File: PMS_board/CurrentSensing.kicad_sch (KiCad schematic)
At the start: 0 parts

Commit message: Added Current Sensing
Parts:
- added C40, C41, C42, C43, C44: 0.1uF, symbol Device:C
- added R36, R37, R38, R39, R40: 0.5m, Package_SON:WSON-8-1EP_6x5mm_P1.27mm_EP3.4x4mm, symbol Device:R_Shunt_US
- added U14, U15, U16, U17, U9: INA186A2QDCKRQ1, DCK0006A-IPC_A, symbol Symbols:INA186A2QDCKRQ1
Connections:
- new net: R36.2, U9.4 (IN+)
- new net: R36.3, U9.5 (IN-)
- new net: R37.2, U14.4 (IN+)
- new net: R37.3, U14.5 (IN-)
- new net: R38.2, U15.4 (IN+)
- new net: R38.3, U15.5 (IN-)
- new net: R40.2, U17.4 (IN+)
- new net: R40.3, U17.5 (IN-)
- new net: R39.2, U16.4 (IN+)
- new net: R39.3, U16.5 (IN-)
- new net +12V: R40.1
- new net +24V: R39.1
- new net +3.3V: C40.1, C41.1, C42.1, C43.1, C44.1, U14.3 (VS), U15.3 (VS), U16.3 (VS), U17.3 (VS), U9.3 (VS)
- new net AUX_OUT: R37.4
- new net AUX_SENSE: U14.6 (OUT)
- new net BATT_IN: R36.1
- new net BATT_OUT: R36.4
- new net BATT_SENSE: U9.6 (OUT)
- new net BOARD_OUT: R38.4
- new net BOARD_SENSE: U15.6 (OUT)
- new net GND: C40.2, C41.2, C42.2, C43.2, C44.2, U14.1 (REF), U14.2 (GND), U15.1 (REF), U15.2 (GND), U16.1 (REF), U16.2 (GND), U17.1 (REF), U17.2 (GND), U9.1 (REF), U9.2 (GND)
- new net JET_OUT: R40.4
- new net JET_SENSE: U17.6 (OUT)
- new net NET_OUT: R39.4
- new net NET_SENSE: U16.6 (OUT)
- new net PACK+: R37.1, R38.1

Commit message: Changed shunt resistor values to be more accurate
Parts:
- R36: value 0.5m -> 0.2m
- R37: value 0.5m -> 2m
- R38, R40: value 0.5m -> 10m
- R39: value 0.5m -> 50m
- U14, U15, U17: value INA186A2QDCKRQ1 -> INA186A2IDCK
- U16: value INA186A2QDCKRQ1 -> INA186A1IDCK
- U9: value INA186A2QDCKRQ1 -> INA186A3IDCK
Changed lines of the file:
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@@
 			)
 		)
-		(property "Value" "0.5m"
+		(property "Value" "0.2m"
 			(at 17.78 59.6899 0)
 			(show_name no)
@@
 			)
 		)
-		(property "Value" "0.5m"
+		(property "Value" "2m"
 			(at 101.6 60.9599 0)
 			(show_name no)
@@
 			)
 		)
-		(property "Value" "INA186A2QDCKRQ1"
+		(property "Value" "INA186A3IDCK"
 			(at 57.15 43.18 0)
 			(show_name no)
@@
 			)
 		)
-		(property "Value" "0.5m"
+		(property "Value" "10m"
 			(at 181.61 60.9599 0)
 			(show_name no)
@@
 			)
 		)
-		(property "Value" "INA186A2QDCKRQ1"
+		(property "Value" "INA186A2IDCK"
 			(at 140.97 109.22 0)
 			(show_name no)
@@
 			)
 		)
-		(property "Value" "0.5m"
+		(property "Value" "50m"
 			(at 17.78 124.4599 0)
 			(show_name no)
@@
 			)
 		)
-		(property "Value" "INA186A2QDCKRQ1"
+		(property "Value" "INA186A2IDCK"
 			(at 140.97 44.45 0)
 			(show_name no)
@@
 			)
 		)
-		(property "Value" "INA186A2QDCKRQ1"
+		(property "Value" "INA186A2IDCK"
 			(at 220.98 44.45 0)
 			(show_name no)
@@
 			)
 		)
-		(property "Value" "INA186A2QDCKRQ1"
+		(property "Value" "INA186A1IDCK"
 			(at 57.15 107.95 0)
 			(show_name no)
@@
 			)
 		)
-		(property "Value" "0.5m"
+		(property "Value" "10m"
 			(at 101.6 125.7299 0)
 			(show_name no)

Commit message: Added ADC for current sensing
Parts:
- removed C41: 0.1uF, symbol Device:C
- removed R37: 2m, Package_SON:WSON-8-1EP_6x5mm_P1.27mm_EP3.4x4mm, symbol Device:R_Shunt_US
- removed U14: INA186A2IDCK, DCK0006A-IPC_A, symbol Symbols:INA186A2QDCKRQ1
- added U18: MCP3204T-CI/ST, Package_DFN_QFN:QFN-20-1EP_5x5mm_P0.65mm_EP3.35x3.35mm, symbol Analog_ADC:MCP3204
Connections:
- net +3.3V: now also U18.13 (Vref), U18.14 (Vdd)
- net BATT_SENSE: now also U18.1 (CH0)
- net GND: now also U18.12 (AGND), U18.7 (DGND)
- net JET_SENSE: now also U18.4 (CH3)
- net NET_SENSE: now also U18.3 (CH2)
- net BOARD_SENSE renamed CORE_SENSE
- net CORE_SENSE: now also U18.2 (CH1)
- new net CLK: U18.11 (CLK)
- new net CS: U18.8 (~{CS}/SHDN)
- new net Din: U18.9 (Din)
- new net Dout: U18.10 (Dout)
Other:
- moved on the sheet: C42, R38, U15

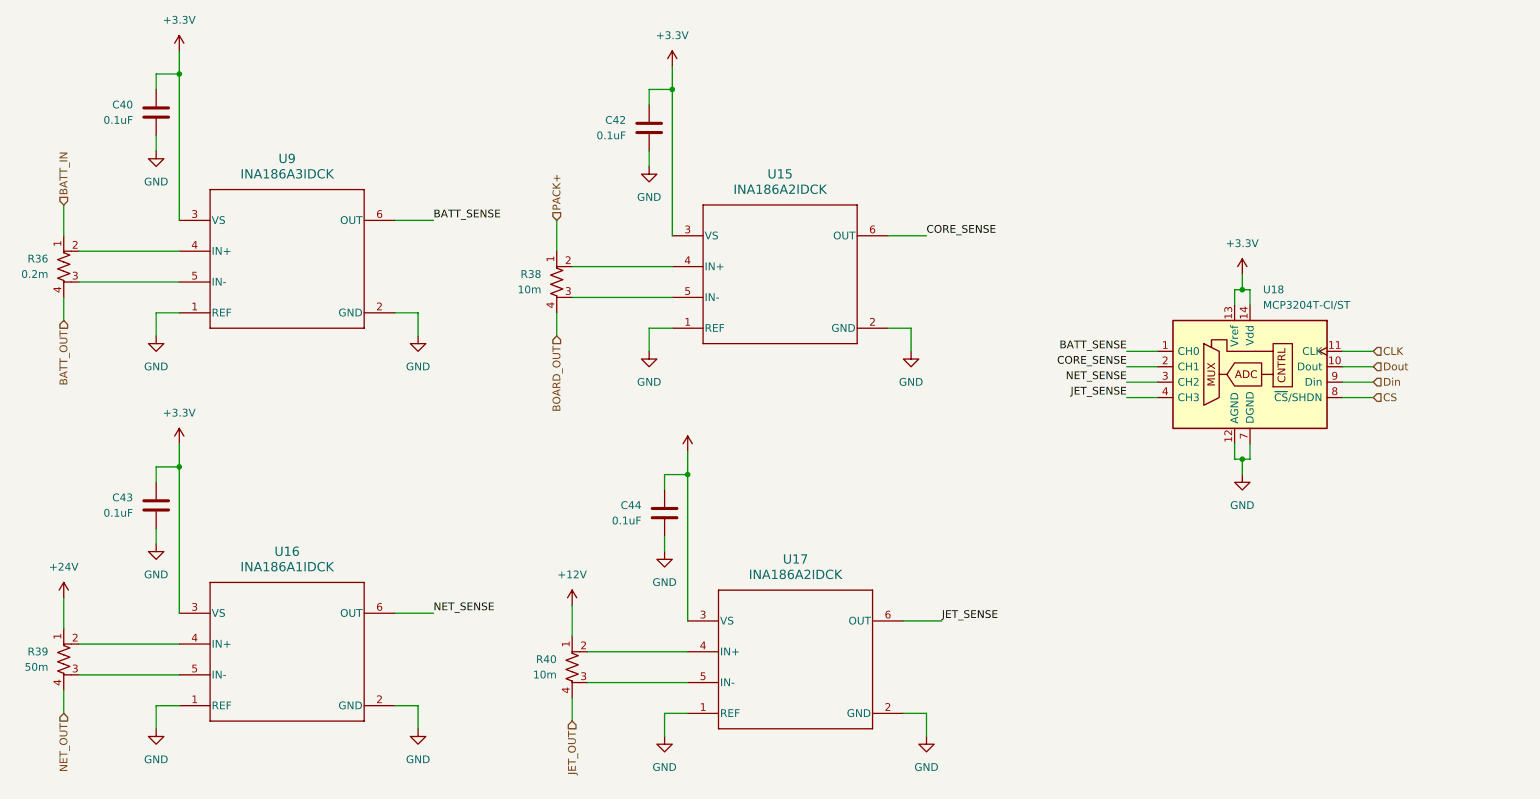
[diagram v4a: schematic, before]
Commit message: Refine Current Sensing
- Removed redundant current sensors
- Fixed hierarchical labelling for sensors
- added labeling for a few circuits
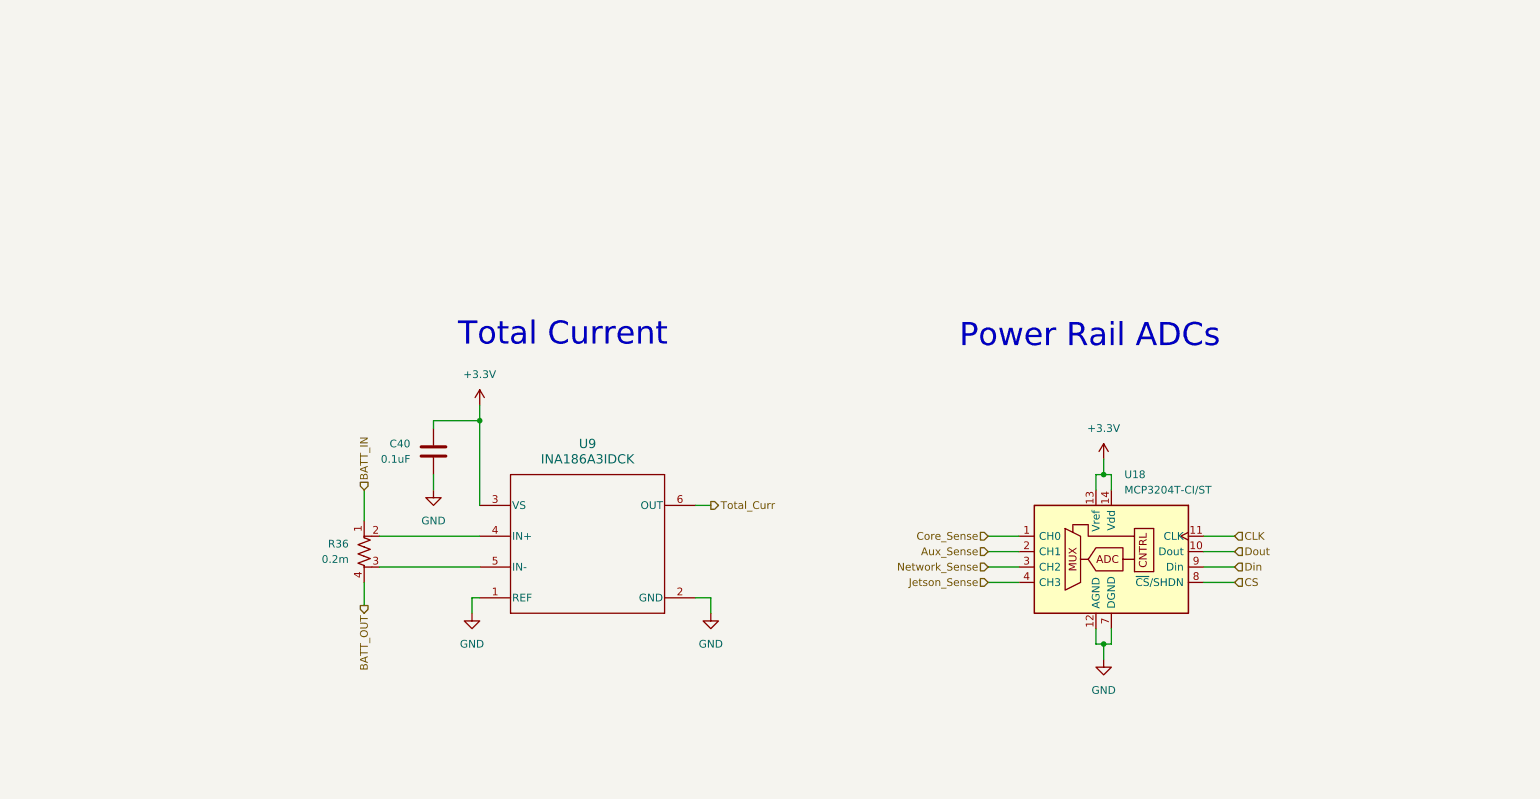
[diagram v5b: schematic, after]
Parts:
- removed C42, C43, C44: 0.1uF, symbol Device:C
- removed R38, R40: 10m, Package_SON:WSON-8-1EP_6x5mm_P1.27mm_EP3.4x4mm, symbol Device:R_Shunt_US
- removed R39: 50m, Package_SON:WSON-8-1EP_6x5mm_P1.27mm_EP3.4x4mm, symbol Device:R_Shunt_US
- removed U15, U17: INA186A2IDCK, DCK0006A-IPC_A, symbol Symbols:INA186A2QDCKRQ1
- removed U16: INA186A1IDCK, DCK0006A-IPC_A, symbol Symbols:INA186A2QDCKRQ1
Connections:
- net BATT_SENSE renamed Core_Sense
- net Core_Sense: no longer U9.6 (OUT)
- net CORE_SENSE renamed Aux_Sense
- net JET_SENSE renamed Jetson_Sense
- net NET_SENSE renamed Network_Sense
- new net Total_Curr: U9.6 (OUT)
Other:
- note added: "Power Rail ADCs"
- note added: "Total Current"
- moved on the sheet: C40, R36, U18, U9

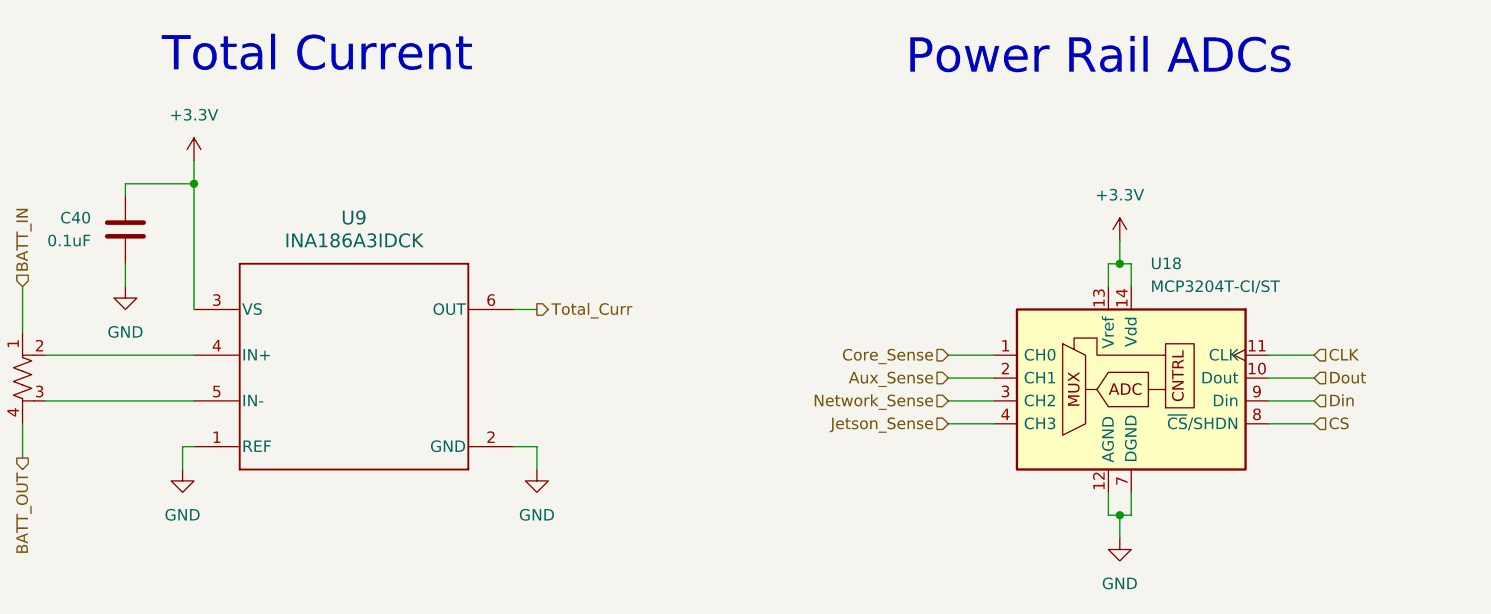
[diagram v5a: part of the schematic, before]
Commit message: Finish Schematic
There's definitely stuff I missed, but I'm tired so we can review later. For my members to keep track of things, these are the changes/last minute additions I ran out of time to teach:
- brake chopper circuitry & reverse voltage protection for aux & motor rails
- microcontroller pinnouts
- net connections between sheets
- voltage resistors & system voltage measurements
- cell sense connectors & switch
- ADC routing
Please Please PLEASE ask questions about these additions. I don't want you guys to feel like you don't own this schematic, and I'm sorry I had to take away some of these designs to finish early. I definitely left too much on your plate to get everything perfect, which is my bad. I will happily walk through each and every circuit and help explain each part so you can better know your project when we get to reviewing and debugging later down the line.
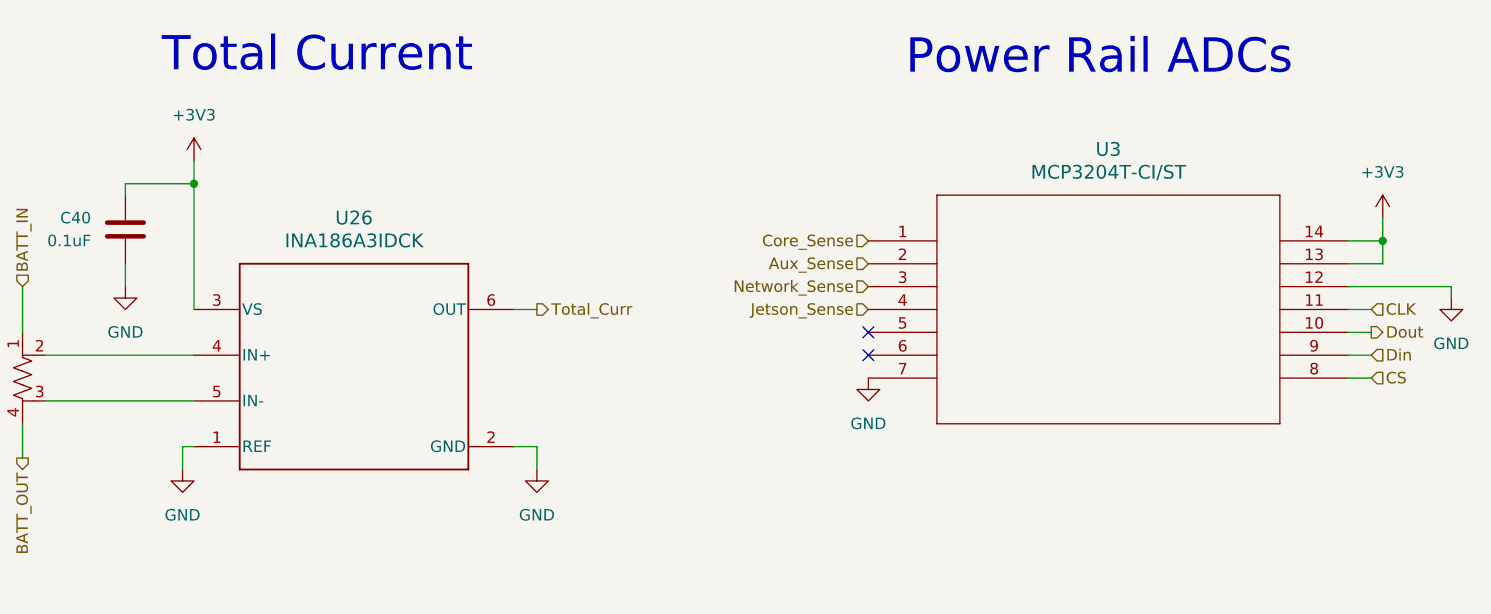
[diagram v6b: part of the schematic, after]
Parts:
- removed U18: MCP3204T-CI/ST, Package_DFN_QFN:QFN-20-1EP_5x5mm_P0.65mm_EP3.35x3.35mm, symbol Analog_ADC:MCP3204
- removed U9: INA186A3IDCK, DCK0006A-IPC_A, symbol Symbols:INA186A2QDCKRQ1
- added U26: INA186A3IDCK, DCK0006A-IPC_A, symbol Symbols:INA186A2QDCKRQ1
- added U3: MCP3204T-CI/ST, TSSOP14_MC_MCH, symbol MCP3204T-CIST:MCP3204T-CI_ST
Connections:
- net Aux_Sense: now also U3.2
- net CLK: now also U3.11
- net CS: now also U3.8
- net Core_Sense: now also U3.1
- net Din: now also U3.9
- net Dout: now also U3.10
- net GND: now also U26.1 (REF), U26.2 (GND), U3.12, U3.7
- net Jetson_Sense: now also U3.4
- net Network_Sense: now also U3.3
- net Total_Curr: now also U26.6 (OUT)
- net at R36.2: now also U26.4 (IN+)
- net at R36.3: now also U26.5 (IN-)
- net +3.3V renamed +3V3
- net +3V3: now also U26.3 (VS), U3.13, U3.14
- no-connect marks 0 -> 2

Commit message: Add Footprints & such
whoops forgot to push yesterday teehee
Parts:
- C40: footprint (none) -> Capacitor_SMD:C_0603_1608Metric
- U26: footprint DCK0006A-IPC_A -> INA186A3IDCK:SO8_DCK_TEX
- U3: footprint TSSOP14_MC_MCH -> MCP3204T-CIST:TSSOP14_MC_MCH
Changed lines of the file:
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@@
 			)
 		)
-		(property "Footprint" ""
+		(property "Footprint" "Capacitor_SMD:C_0603_1608Metric"
 			(at 80.3148 92.71 0)
 			(hide yes)
@@
 			)
 		)
-		(property "Footprint" "TSSOP14_MC_MCH"
+		(property "Footprint" "MCP3204T-CIST:TSSOP14_MC_MCH"
 			(at 163.83 90.17 0)
 			(hide yes)
@@
 			)
 		)
-		(property "Footprint" "DCK0006A-IPC_A"
+		(property "Footprint" "INA186A3IDCK:SO8_DCK_TEX"
 			(at 88.9 97.79 0)
 			(hide yes)

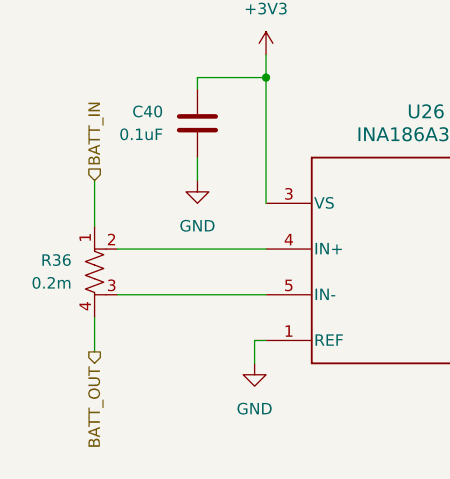
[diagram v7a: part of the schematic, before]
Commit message: Minor component tweaks and added a seperate LED sheet
Changed component values
Added labels
Moved LEDs to it's own sheet
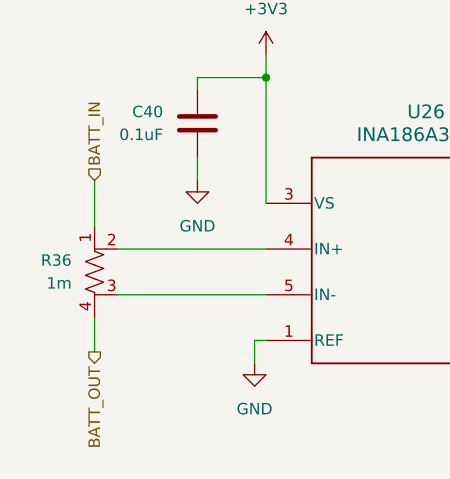
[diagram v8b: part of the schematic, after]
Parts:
- R36: value 0.2m -> 1m
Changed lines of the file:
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@@
 			)
 		)
-		(property "Value" "0.2m"
+		(property "Value" "1m"
 			(at 67.31 106.6799 0)
 			(show_name no)
